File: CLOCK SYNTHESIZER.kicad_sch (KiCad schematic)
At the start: 40 parts, among them U1 CK100/133, Y1 14.318MHz

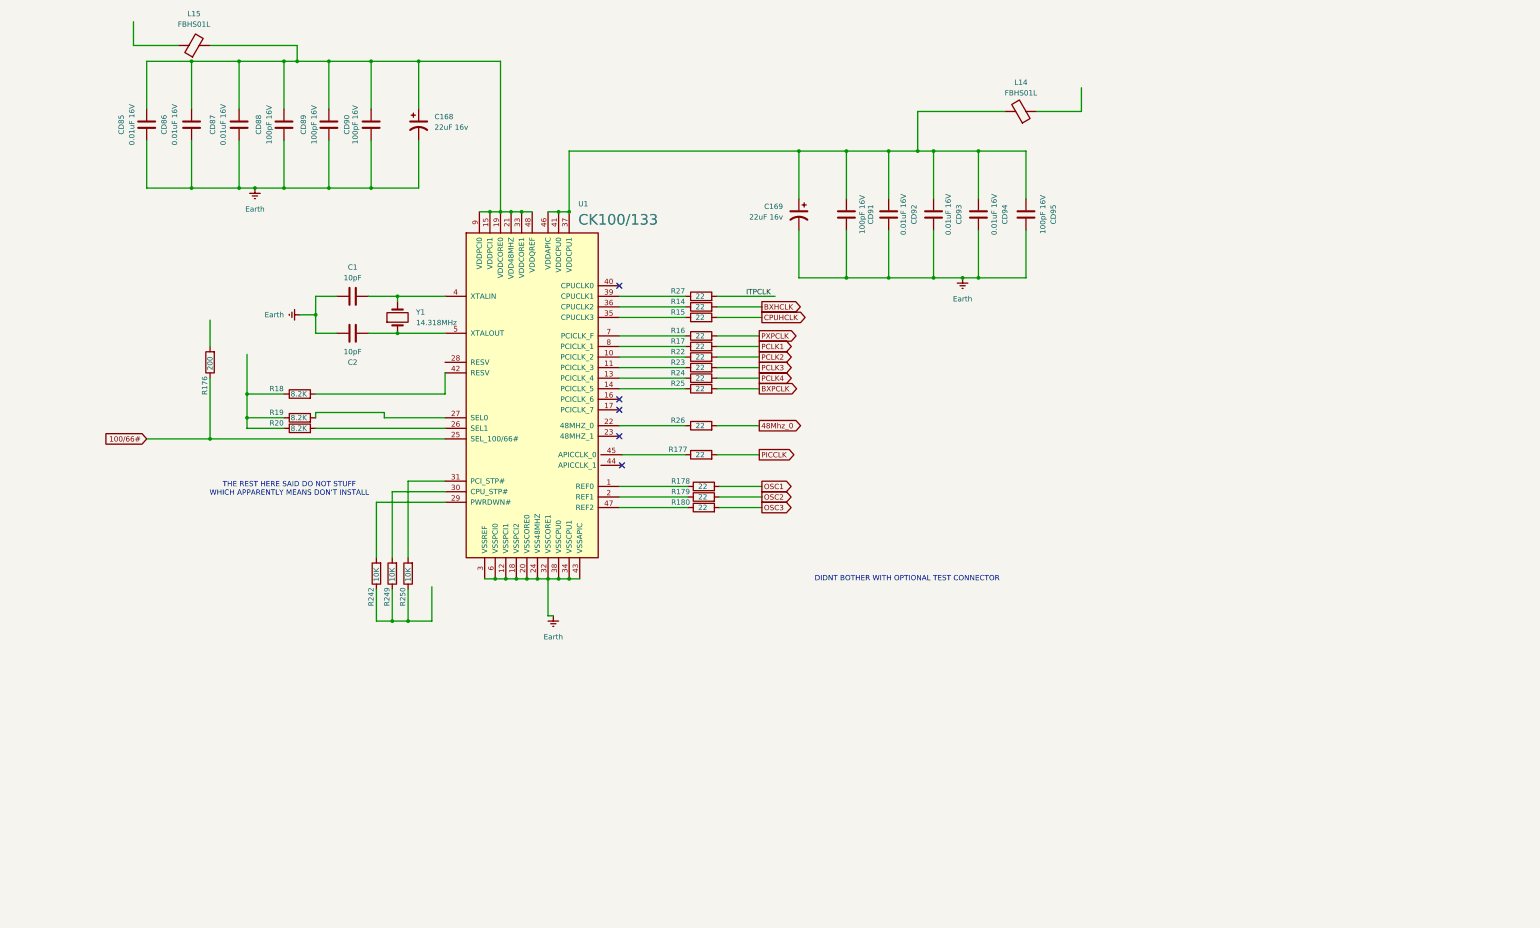
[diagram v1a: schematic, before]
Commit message: page 6 CLOCK SYNTHESIZER done
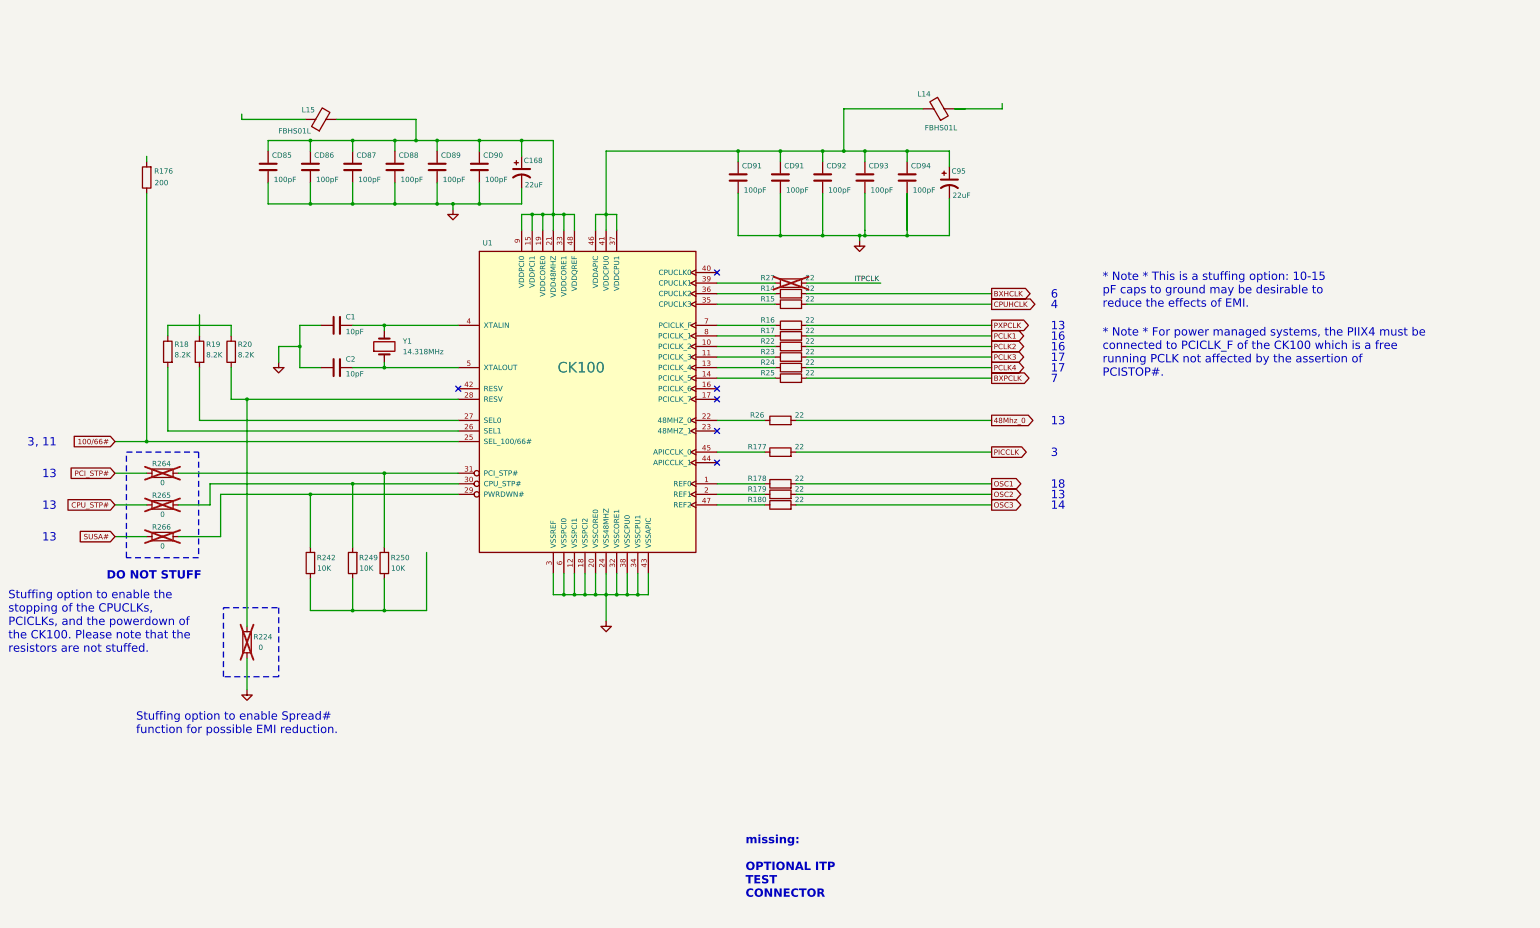
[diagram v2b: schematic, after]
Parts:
- removed C169: 22uF 16v, Capacitor_SMD:C_0201_0603Metric, symbol Device:C_Polarized_US
- removed CD91, CD95: 100pF 16V, Capacitor_SMD:C_0201_0603Metric, symbol Device:C
- added C95: 22uF, Capacitor_SMD:C_0201_0603Metric, symbol Device:C_Polarized_US
- added CD91 (x2): 100pF, Capacitor_SMD:C_0201_0603Metric, symbol Device:C
- added R224, R264, R265, R266: 0, Resistor_SMD:R_0201_0603Metric, symbol Device:R
- C168: value 22uF 16v -> 22uF
- CD85, CD86, CD87, CD92, CD93, CD94: value 0.01uF 16V -> 100pF
- CD88, CD89, CD90: value 100pF 16V -> 100pF
- R27: now not fitted
- U1: value CK100/133 -> CK100; symbol P2-3_era:CK100/133 -> P2-3_era:CK100
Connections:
- net at R18.1, R20.1: no longer R19.1
- net at R249.2, U1.30 (CPU_STP#): now also R265.2
- net at CD92.1, CD93.1, CD94.1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: now also C95.1, CD91.1, CD91.1
- net at R250.2, U1.31 (PCI_STP#): now also R264.2
- net at R18.2: now also U1.26 (SEL1); no longer U1.42 (RESV)
- net at R20.2: now also U1.28 (RESV), R224.2; no longer U1.26 (SEL1)
- net at R242.2, U1.29 (PWRDWN#): now also R266.2
- net Earth renamed GND
- net GND: now also C95.2, CD91.2, CD91.2, R224.1
- new net CPU_STP#: R265.1
- new net PCI_STP#: R264.1
- new net SUSA#: R266.1
- no-connect marks 5 -> 6
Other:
- note added: "* Note * For power managed systems, the PIIX4 must be connected to PCICLK_F of the CK100 which is a free running PCLK not affected by the assertion of PCISTOP#."
- note added: "* Note * This is a stuffing option: 10-15 pF caps to ground may be desirable to reduce the effects of EMI."
- note added: ","
- note added: "11"
- note added: "13"
- note added: "14"
- note added: "16"
- note added: "17"
- note added: "18"
- note added: "3"
- note added: "4"
- note added: "6"
- note added: "7"
- note added: "DO NOT STUFF"
- note added: "Stuffing option to enable Spread# function for possible EMI reduction."
- note added: "Stuffing option to enable the stopping of the CPUCLKs, PCICLKs, and the powerdown of the CK100. Please note that the resistors are not stuffed."
- note added: "missing: OPTIONAL ITP TEST CONNECTOR"
- note removed: "DIDNT BOTHER WITH OPTIONAL TEST CONNECTOR"
- note removed: "THE REST HERE SAID DO NOT STUFF WHICH APPARENTLY MEANS DON'T INSTALL"
- moved on the sheet: C1, C168, C2, L14, L15, R14, R15, R16, R17, R176, R177, R178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

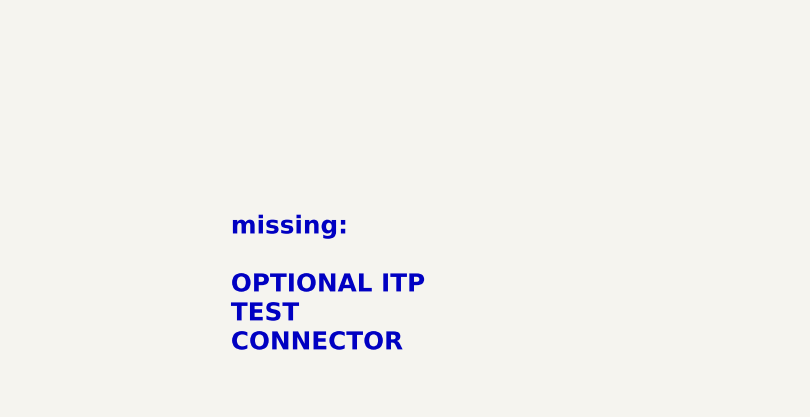
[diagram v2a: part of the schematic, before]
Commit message: pages 9 10 11 DIMM socket and DIMM socket symbol
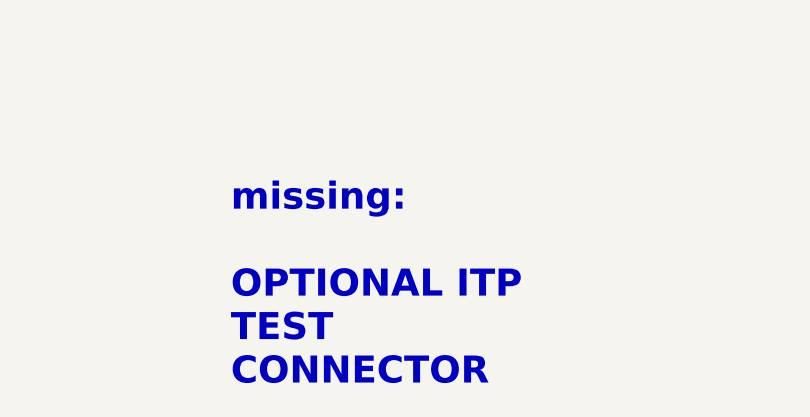
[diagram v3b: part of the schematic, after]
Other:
- title: (none) -> CLOCK SYNTHESIZER
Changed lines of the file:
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@@
 	(paper "User" 380 300)
 	(title_block
+		(title "CLOCK SYNTHESIZER")
 		(date "Thursday, April 09, 1998")
 		(rev "1.0")
@@
 		(effects
 			(font
-				(size 2 2)
+				(size 3 3)
 				(thickness 0.4)
 				(bold yes)
